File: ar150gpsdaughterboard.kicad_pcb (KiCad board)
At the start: 2 copper layers, 30.5 x 19.2 mm, 7 parts, among them P1 CONN_02X05, Q1 BSS138, U1 QUECTEL-L80

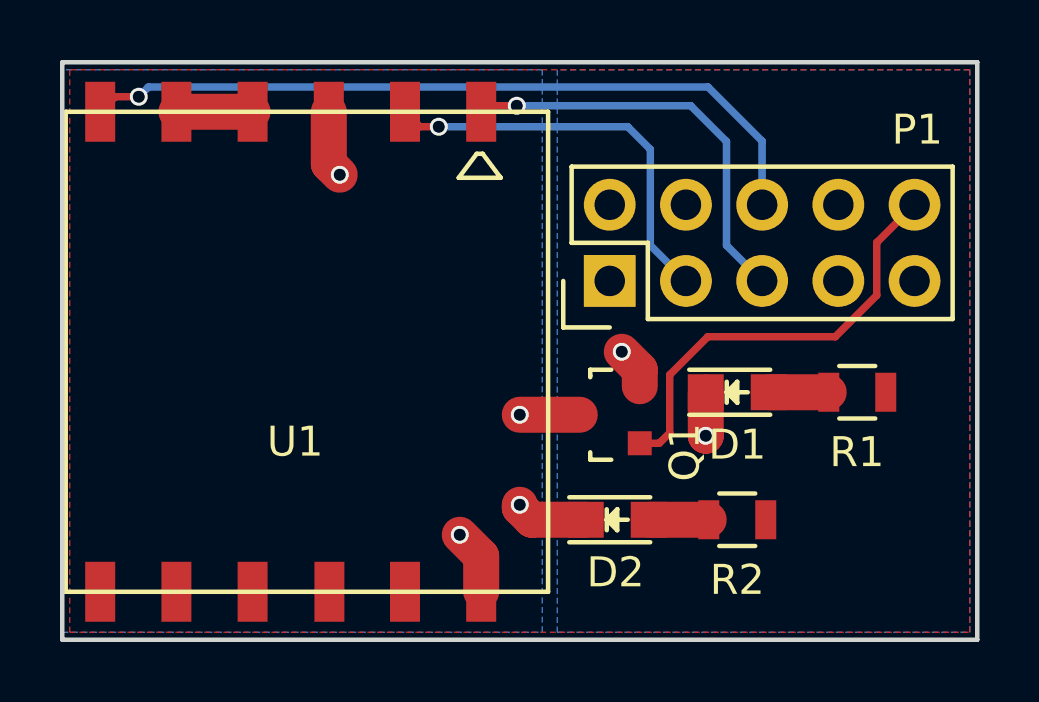
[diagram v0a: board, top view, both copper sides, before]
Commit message: updated pinout of the ar150 pin header
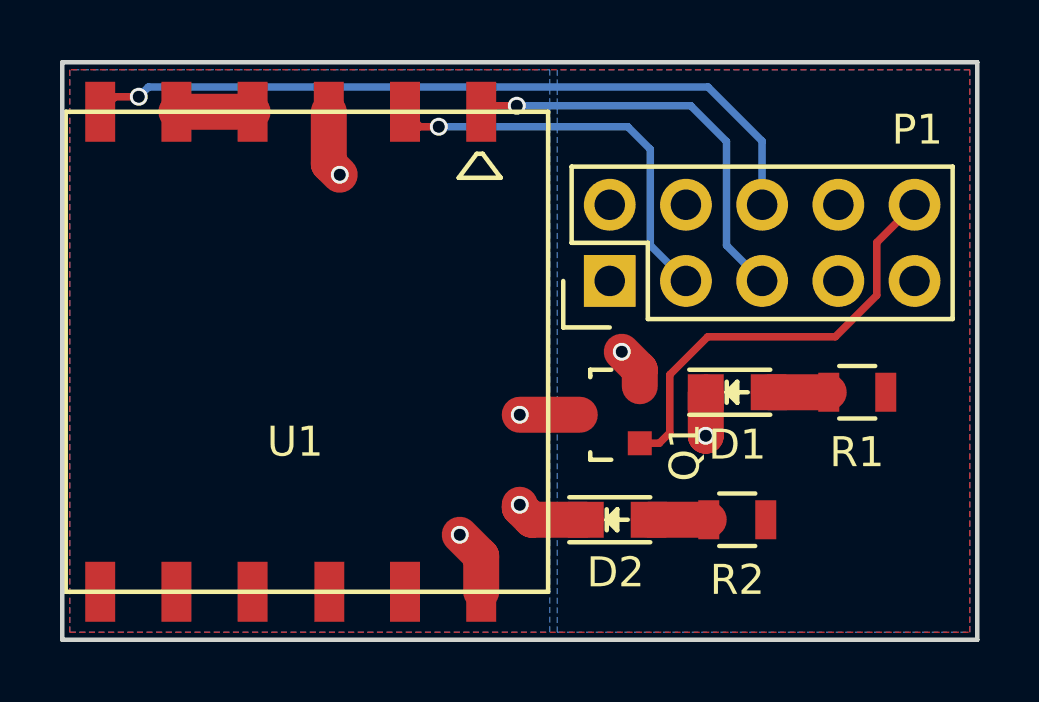
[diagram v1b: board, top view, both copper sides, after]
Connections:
- P1 pad 7: GND -> (no net)
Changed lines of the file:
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@@
 (kicad_pcb (version 4) (host pcbnew 4.0.2+dfsg1-stable)
   (general
-    (links 17)
-    (no_connects 0)
-    (area 118.589999 91.125 152.922 120.9815)
+    (links 16)
+    (no_connects 9)
+    (area 118.674999 95.174999 149.325001 114.575001)
     (thickness 1.6)
-    (drawings 7)
+    (drawings 8)
     (tracks 51)
     (zones 0)
@@
     (pad 6 thru_hole oval (at 2.54 5.08 90) (size 1.7272 1.7272) (drill 1.016) (layers *.Cu *.Mask F.SilkS)
       (net 7 GP_14))
-    (pad 7 thru_hole oval (at 0 7.62 90) (size 1.7272 1.7272) (drill 1.016) (layers *.Cu *.Mask F.SilkS)
-      (net 2 GND))
+    (pad 7 thru_hole oval (at 0 7.62 90) (size 1.7272 1.7272) (drill 1.016) (layers *.Cu *.Mask F.SilkS))
     (pad 8 thru_hole oval (at 2.54 7.62 90) (size 1.7272 1.7272) (drill 1.016) (layers *.Cu *.Mask F.SilkS))
     (pad 9 thru_hole oval (at 0 10.16 90) (size 1.7272 1.7272) (drill 1.016) (layers *.Cu *.Mask F.SilkS)
@@
   )
   (dimension 19.25 (width 0.3) (layer Cmts.User)
-    (gr_text "19.250 mm" (at 156.35 104.875 270) (layer Cmts.User)
+    (gr_text "19.250 mm" (at 113.15 104.875 270) (layer Cmts.User)
       (effects (font (size 1.5 1.5) (thickness 0.3)))
     )
-    (feature1 (pts (xy 150 114.5) (xy 157.7 114.5)))
-    (feature2 (pts (xy 150 95.25) (xy 157.7 95.25)))
-    (crossbar (pts (xy 155 95.25) (xy 155 114.5)))
-    (arrow1a (pts (xy 155 114.5) (xy 154.413579 113.373496)))
-    (arrow1b (pts (xy 155 114.5) (xy 155.586421 113.373496)))
-    (arrow2a (pts (xy 155 95.25) (xy 154.413579 96.376504)))
-    (arrow2b (pts (xy 155 95.25) (xy 155.586421 96.376504)))
+    (feature1 (pts (xy 117.5 114.5) (xy 111.8 114.5)))
+    (feature2 (pts (xy 117.5 95.25) (xy 111.8 95.25)))
+    (crossbar (pts (xy 114.5 95.25) (xy 114.5 114.5)))
+    (arrow1a (pts (xy 114.5 114.5) (xy 113.913579 113.373496)))
+    (arrow1b (pts (xy 114.5 114.5) (xy 115.086421 113.373496)))
+    (arrow2a (pts (xy 114.5 95.25) (xy 113.913579 96.376504)))
+    (arrow2b (pts (xy 114.5 95.25) (xy 115.086421 96.376504)))
+  )
+  (dimension 4.75 (width 0.3) (layer Cmts.User)
+    (gr_text "4.750 mm" (at 159.85 97.625 270) (layer Cmts.User)
+      (effects (font (size 1.5 1.5) (thickness 0.3)))
+    )
+    (feature1 (pts (xy 150.5 100) (xy 161.2 100)))
+    (feature2 (pts (xy 150.5 95.25) (xy 161.2 95.25)))
+    (crossbar (pts (xy 158.5 95.25) (xy 158.5 100)))
+    (arrow1a (pts (xy 158.5 100) (xy 157.913579 98.873496)))
+    (arrow1b (pts (xy 158.5 100) (xy 159.086421 98.873496)))
+    (arrow2a (pts (xy 158.5 95.25) (xy 157.913579 96.376504)))
+    (arrow2b (pts (xy 158.5 95.25) (xy 159.086421 96.376504)))
   )
   (dimension 30.5 (width 0.3) (layer Cmts.User)
@@
     (polygon
       (pts
-        (xy 118.75 95.5) (xy 118.75 114.25) (xy 134.75 114.25) (xy 134.75 95.5)
+        (xy 119 95.5) (xy 119 114.25) (xy 135 114.25) (xy 135 95.5)
       )
     )

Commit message: new board with a pps line indicator
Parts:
- added D3: LED, LEDs:LED_0805, F.Cu at (143.2, 97.0)
- added R3: 300, Resistors_SMD:R_0805, F.Cu at (137.2, 97.0)
- R1, R2: value R -> 300
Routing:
- net Net-(D3-Pad2): track 0.00 -> 4.00 mm
- net GP_14: track 25.3 -> 26.7 mm, vias 1 -> 2
- net GND: track 2.85 -> 4.05 mm, vias 2 -> 3
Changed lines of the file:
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@@
 (kicad_pcb (version 4) (host pcbnew 4.0.2+dfsg1-stable)
   (general
-    (links 16)
-    (no_connects 9)
-    (area 118.674999 95.174999 149.325001 114.575001)
+    (links 19)
+    (no_connects 0)
+    (area 106.500001 87.65 165.785715 116.975)
     (thickness 1.6)
     (drawings 8)
-    (tracks 51)
+    (tracks 58)
     (zones 0)
-    (modules 7)
-    (nets 10)
+    (modules 9)
+    (nets 11)
   )
   (page A4)
@@
   (net 8 +3V3)
   (net 9 GP_17)
+  (net 10 "Net-(D3-Pad2)")
   (net_class Default "This is the default net class."
     (clearance 0.2)
@@
     (add_net "Net-(D1-Pad2)")
     (add_net "Net-(D2-Pad2)")
+    (add_net "Net-(D3-Pad2)")
     (add_net RX)
     (add_net TX)
@@
       (effects (font (size 1 1) (thickness 0.15)))
     )
-    (fp_text value LED (at 0.193 9.5065) (layer F.Fab)
+    (fp_text value LED (at 0.193 5.5) (layer F.Fab)
       (effects (font (size 1 1) (thickness 0.15)))
     )
@@
     (descr "Through hole pin header")
     (tags "pin header")
-    (fp_text reference P1 (at 5.04 10.25 180) (layer F.SilkS)
+    (fp_text reference P1 (at -2.21 10.5 180) (layer F.SilkS)
       (effects (font (size 1 1) (thickness 0.15)))
     )
@@
       (effects (font (size 1 1) (thickness 0.15)))
     )
-    (fp_text value R (at -4.75 0.255 180) (layer F.Fab)
+    (fp_text value 300 (at -6 3 180) (layer F.Fab)
       (effects (font (size 1 1) (thickness 0.15)))
     )
@@
       (effects (font (size 1 1) (thickness 0.15)))
     )
-    (fp_text value R (at -9.0045 -0.0065 180) (layer F.Fab)
+    (fp_text value 300 (at 0 -5.5 180) (layer F.Fab)
       (effects (font (size 1 1) (thickness 0.15)))
     )
@@
       (net 4 GP_GND))
   )
+  (module LEDs:LED_0805 (layer F.Cu)
+    (at 143.25 97 180)
+    (descr "LED 0805 smd package")
+    (tags "LED 0805 SMD")
+    (attr smd)
+    (fp_text reference D3 (at -3.5 -0.25 180) (layer F.SilkS)
+      (effects (font (size 1 1) (thickness 0.15)))
+    )
+    (fp_text value LED (at 0 3 180) (layer F.Fab)
+      (effects (font (size 1 1) (thickness 0.15)))
+    )
+    (fp_line (start -1.6 0.75) (end 1.1 0.75) (layer F.SilkS) (width 0.15))
+    (fp_line (start -1.6 -0.75) (end 1.1 -0.75) (layer F.SilkS) (width 0.15))
+    (fp_line (start -0.1 0.15) (end -0.1 -0.1) (layer F.SilkS) (width 0.15))
+    (fp_line (start -0.1 -0.1) (end -0.25 0.05) (layer F.SilkS) (width 0.15))
+    (fp_line (start -0.35 -0.35) (end -0.35 0.35) (layer F.SilkS) (width 0.15))
+    (fp_line (start 0 0) (end 0.35 0) (layer F.SilkS) (width 0.15))
+    (fp_line (start -0.35 0) (end 0 -0.35) (layer F.SilkS) (width 0.15))
+    (fp_line (start 0 -0.35) (end 0 0.35) (layer F.SilkS) (width 0.15))
+    (fp_line (start 0 0.35) (end -0.35 0) (layer F.SilkS) (width 0.15))
+    (fp_line (start 1.9 -0.95) (end 1.9 0.95) (layer F.CrtYd) (width 0.05))
+    (fp_line (start 1.9 0.95) (end -1.9 0.95) (layer F.CrtYd) (width 0.05))
+    (fp_line (start -1.9 0.95) (end -1.9 -0.95) (layer F.CrtYd) (width 0.05))
+    (fp_line (start -1.9 -0.95) (end 1.9 -0.95) (layer F.CrtYd) (width 0.05))
+    (pad 2 smd rect (at 1.04902 0) (size 1.19888 1.19888) (layers F.Cu F.Paste F.Mask)
+      (net 10 "Net-(D3-Pad2)"))
+    (pad 1 smd rect (at -1.04902 0) (size 1.19888 1.19888) (layers F.Cu F.Paste F.Mask)
+      (net 2 GND))
+    (model LEDs.3dshapes/LED_0805.wrl
+      (at (xyz 0 0 0))
+      (scale (xyz 1 1 1))
+      (rotate (xyz 0 0 0))
+    )
+  )
+  (module Resistors_SMD:R_0805 (layer F.Cu)
+    (at 137.25 97)
+    (descr "Resistor SMD 0805, reflow soldering, Vishay (see dcrcw.pdf)")
+    (tags "resistor 0805")
+    (attr smd)
+    (fp_text reference R3 (at 2.75 0 90) (layer F.SilkS)
+      (effects (font (size 1 1) (thickness 0.15)))
+    )
+    (fp_text value 300 (at 0 2.1) (layer F.Fab)
+      (effects (font (size 1 1) (thickness 0.15)))
+    )
+    (fp_line (start -1.6 -1) (end 1.6 -1) (layer F.CrtYd) (width 0.05))
+    (fp_line (start -1.6 1) (end 1.6 1) (layer F.CrtYd) (width 0.05))
+    (fp_line (start -1.6 -1) (end -1.6 1) (layer F.CrtYd) (width 0.05))
+    (fp_line (start 1.6 -1) (end 1.6 1) (layer F.CrtYd) (width 0.05))
+    (fp_line (start 0.6 0.875) (end -0.6 0.875) (layer F.SilkS) (width 0.15))
+    (fp_line (start -0.6 -0.875) (end 0.6 -0.875) (layer F.SilkS) (width 0.15))
+    (pad 1 smd rect (at -0.95 0) (size 0.7 1.3) (layers F.Cu F.Paste F.Mask)
+      (net 7 GP_14))
+    (pad 2 smd rect (at 0.95 0) (size 0.7 1.3) (layers F.Cu F.Paste F.Mask)
+      (net 10 "Net-(D3-Pad2)"))
+    (model Resistors_SMD.3dshapes/R_0805.wrl
+      (at (xyz 0 0 0))
+      (scale (xyz 1 1 1))
+      (rotate (xyz 0 0 0))
+    )
+  )
   (dimension 19.25 (width 0.3) (layer Cmts.User)
     (gr_text "19.250 mm" (at 113.15 104.875 270) (layer Cmts.User)
@@
   (gr_line (start 118.75 95.25) (end 118.75 114.5) (layer Edge.Cuts) (width 0.15))
   (segment (start 142.29902 106.25) (end 144.3 106.25) (width 1.2) (layer F.Cu) (net 1))
+  (segment (start 144.29902 97) (end 145.5 97) (width 0.25) (layer F.Cu) (net 2))
+  (via (at 145.5 97) (size 0.6) (drill 0.4) (layers F.Cu B.Cu) (net 2))
   (segment (start 138.00076 106.05) (end 138.00076 105.50076) (width 1.2) (layer F.Cu) (net 2))
   (segment (start 138.00076 105.50076) (end 137.4 104.9) (width 1.2) (layer F.Cu) (net 2))
@@
   (segment (start 142.08 102.54) (end 140.891399 101.351399) (width 0.25) (layer B.Cu) (net 6))
   (segment (start 140.891399 101.351399) (end 140.891399 97.891399) (width 0.25) (layer B.Cu) (net 6))
+  (segment (start 140.274998 96.074998) (end 135.25 96.074998) (width 0.25) (layer B.Cu) (net 7))
+  (segment (start 135.25 96.074998) (end 121.625002 96.074998) (width 0.25) (layer B.Cu) (net 7))
+  (segment (start 136.3 97) (end 136.175002 97) (width 0.25) (layer F.Cu) (net 7))
+  (via (at 135.25 96.074998) (size 0.6) (drill 0.4) (layers F.Cu B.Cu) (net 7))
+  (segment (start 136.175002 97) (end 135.25 96.074998) (width 0.25) (layer F.Cu) (net 7))
   (segment (start 121.625002 96.074998) (end 121.599999 96.100001) (width 0.25) (layer B.Cu) (net 7))
-  (segment (start 140.274998 96.074998) (end 121.625002 96.074998) (width 0.25) (layer B.Cu) (net 7))
   (segment (start 142.08 97.88) (end 140.274998 96.074998) (width 0.25) (layer B.Cu) (net 7))
   (segment (start 142.08 100) (end 142.08 97.88) (width 0.25) (layer B.Cu) (net 7))
@@
   (segment (start 138.00076 107.95) (end 138.65081 107.95) (width 0.25) (layer F.Cu) (net 9))
   (segment (start 138.65081 107.95) (end 139 107.60081) (width 0.25) (layer F.Cu) (net 9))
+  (segment (start 138.2 97) (end 142.20098 97) (width 0.25) (layer F.Cu) (net 10))
   (zone (net 4) (net_name GP_GND) (layer B.Cu) (hatch edge 0.508)
     (connect_pads yes (clearance 0.3))
